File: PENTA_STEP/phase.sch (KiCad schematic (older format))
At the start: 12 parts, among them Q1 BUK9K45-100E,115, Q2 BUK9K45-100E,115

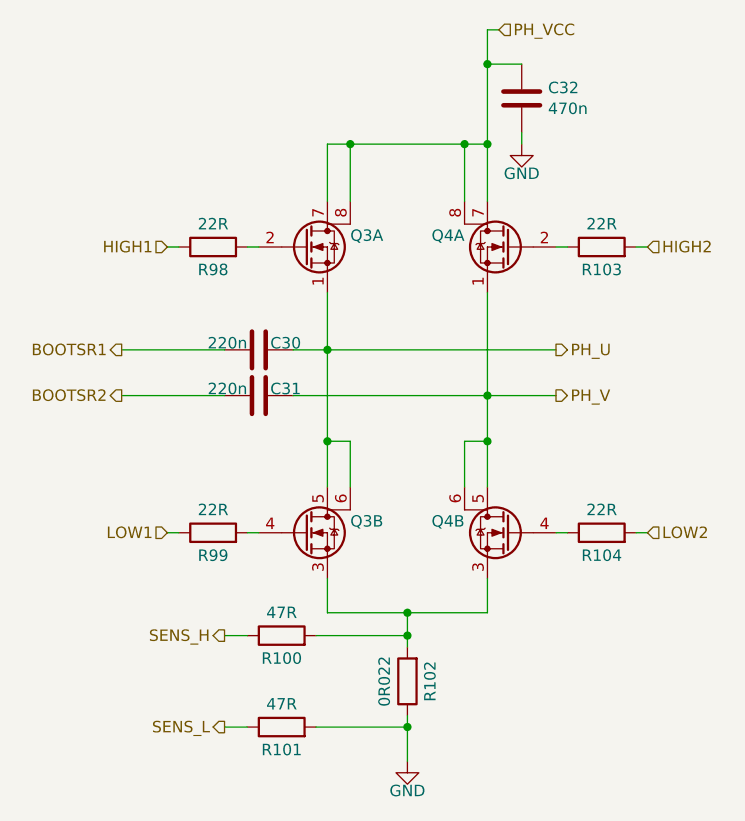
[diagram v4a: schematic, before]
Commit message: finalized BOM, found TMC5160-TA being replaced by TMC5160A-TA
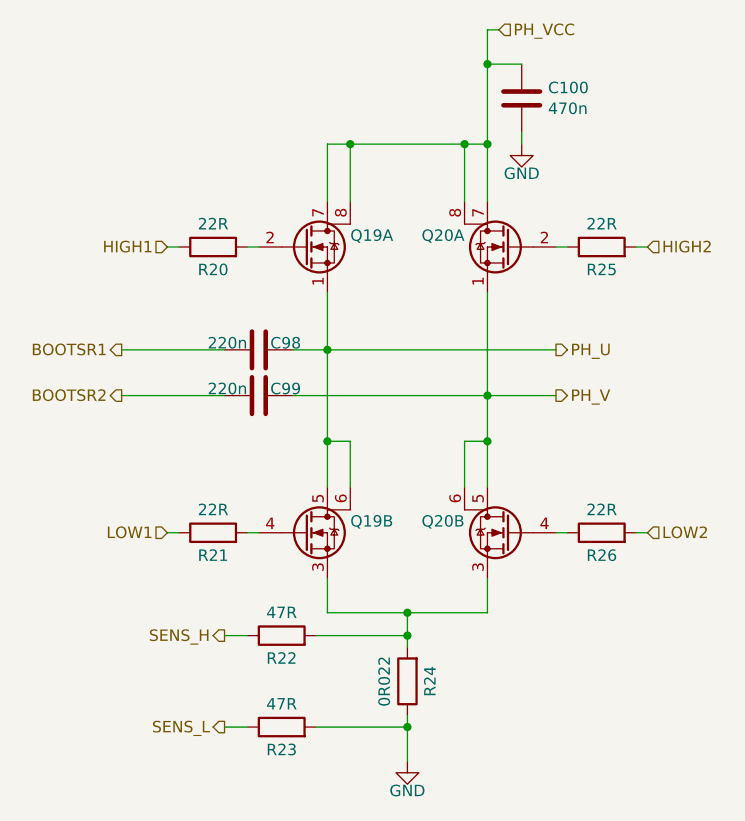
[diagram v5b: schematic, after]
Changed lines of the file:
@@
 EESchema Schematic File Version 4
-LIBS:PENTA_STEP-cache
-EELAYER 26 0
+EELAYER 30 0
 EELAYER END
 $Descr A4 11693 8268
 encoding utf-8
-Sheet 15 16
+Sheet 13 16
 Title ""
 Date ""
@@
 AR Path="/5F24B60D/5E4B900F/5E30367B" Ref="Q17"  Part="1"
 AR Path="/5F24B60D/5E4B9032/5E30367B" Ref="Q19"  Part="1"
-F 0 "Q3" H 5400 3000 50  0000 L CNN
+F 0 "Q19" H 5400 3000 50  0000 L CNN
 F 1 "BUK9K45-100E,115" H 5487 2905 50  0001 L CNN
 F 2 "CUSTOM_FP:TRANS_BUK7K12-60EX" H 5400 2875 50  0001 L CIN
@@
 AR Path="/5F24B60D/5E4B900F/5E303682" Ref="Q18"  Part="1"
 AR Path="/5F24B60D/5E4B9032/5E303682" Ref="Q20"  Part="1"
-F 0 "Q4" H 6300 3000 50  0000 L CNN
+F 0 "Q20" H 6300 3000 50  0000 L CNN
 F 1 "BUK9K45-100E,115" H 6388 2905 50  0001 L CNN
 F 2 "CUSTOM_FP:TRANS_BUK7K12-60EX" H 6300 2875 50  0001 L CIN
@@
 AR Path="/5F24B60D/5E4B900F/5E303689" Ref="Q17"  Part="2"
 AR Path="/5F24B60D/5E4B9032/5E303689" Ref="Q19"  Part="2"
-F 0 "Q3" H 5400 4250 50  0000 L CNN
+F 0 "Q19" H 5400 4250 50  0000 L CNN
 F 1 "BUK9K45-100E,115" H 5487 4155 50  0001 L CNN
 F 2 "CUSTOM_FP:TRANS_BUK7K12-60EX" H 5400 4125 50  0001 L CIN
@@
 AR Path="/5F24B60D/5E4B900F/5E303690" Ref="Q18"  Part="2"
 AR Path="/5F24B60D/5E4B9032/5E303690" Ref="Q20"  Part="2"
-F 0 "Q4" H 6300 4250 50  0000 L CNN
+F 0 "Q20" H 6300 4250 50  0000 L CNN
 F 1 "BUK9K45-100E,115" H 6388 4155 50  0001 L CNN
 F 2 "CUSTOM:TRANS_BUK7K12-60EX" H 6300 4125 50  0001 L CIN
@@
 AR Path="/5F24B60D/5E4B900F/5E303697" Ref="#PWR0109"  Part="1"
 AR Path="/5F24B60D/5E4B9032/5E303697" Ref="#PWR0111"  Part="1"
-F 0 "#PWR045" H 5650 4950 50  0001 C CNN
+F 0 "#PWR0111" H 5650 4950 50  0001 C CNN
 F 1 "GND" H 5650 5100 50  0000 C TNN
 F 2 "" H 5650 5200 50  0001 C CNN
@@
 AR Path="/5F24B60D/5E4B900F/5E30369F" Ref="R17"  Part="1"
 AR Path="/5F24B60D/5E4B9032/5E30369F" Ref="R24"  Part="1"
-F 0 "R102" V 5550 4850 50  0000 C CNN
+F 0 "R24" V 5550 4850 50  0000 C CNN
 F 1 "0R022" V 5750 4850 50  0000 C CNN
 F 2 "CUSTOM_FP:WSH2818R0500FEA" V 5580 4850 50  0001 C CNN
@@
 AR Path="/5F24B60D/5E4B900F/5E3036A9" Ref="R14"  Part="1"
 AR Path="/5F24B60D/5E4B9032/5E3036A9" Ref="R21"  Part="1"
-F 0 "R99" V 4700 4200 50  0000 C CNN
+F 0 "R21" V 4700 4200 50  0000 C CNN
 F 1 "22R" V 4900 4200 50  0000 C CNN
 F 2 "Resistor_SMD:R_0603_1608Metric_Pad1.05x0.95mm_HandSolder" V 4730 4200 50  0001 C CNN
@@
 AR Path="/5F24B60D/5E4B900F/5E3036B3" Ref="R19"  Part="1"
 AR Path="/5F24B60D/5E4B9032/5E3036B3" Ref="R26"  Part="1"
-F 0 "R104" V 6400 4200 50  0000 C CNN
+F 0 "R26" V 6400 4200 50  0000 C CNN
 F 1 "22R" V 6600 4200 50  0000 C CNN
 F 2 "Resistor_SMD:R_0603_1608Metric_Pad1.05x0.95mm_HandSolder" V 6430 4200 50  0001 C CNN
@@
 AR Path="/5F24B60D/5E4B900F/5E3036BD" Ref="R18"  Part="1"
 AR Path="/5F24B60D/5E4B9032/5E3036BD" Ref="R25"  Part="1"
-F 0 "R103" V 6400 2950 50  0000 C CNN
+F 0 "R25" V 6400 2950 50  0000 C CNN
 F 1 "22R" V 6600 2950 50  0000 C CNN
 F 2 "Resistor_SMD:R_0603_1608Metric_Pad1.05x0.95mm_HandSolder" V 6430 2950 50  0001 C CNN
@@
 AR Path="/5F24B60D/5E4B900F/5E3036C7" Ref="R13"  Part="1"
 AR Path="/5F24B60D/5E4B9032/5E3036C7" Ref="R20"  Part="1"
-F 0 "R98" V 4700 2950 50  0000 C CNN
+F 0 "R20" V 4700 2950 50  0000 C CNN
 F 1 "22R" V 4900 2950 50  0000 C CNN
 F 2 "Resistor_SMD:R_0603_1608Metric_Pad1.05x0.95mm_HandSolder" V 4730 2950 50  0001 C CNN
@@
 AR Path="/5F24B60D/5E4B900F/5E3036D1" Ref="R15"  Part="1"
 AR Path="/5F24B60D/5E4B9032/5E3036D1" Ref="R22"  Part="1"
-F 0 "R100" V 5000 4650 50  0000 C CNN
+F 0 "R22" V 5000 4650 50  0000 C CNN
 F 1 "47R" V 5200 4650 50  0000 C CNN
 F 2 "Resistor_SMD:R_0603_1608Metric_Pad1.05x0.95mm_HandSolder" V 5030 4650 50  0001 C CNN
@@
 AR Path="/5F24B60D/5E4B900F/5E3036DB" Ref="R16"  Part="1"
 AR Path="/5F24B60D/5E4B9032/5E3036DB" Ref="R23"  Part="1"
-F 0 "R101" V 5000 5050 50  0000 C CNN
+F 0 "R23" V 5000 5050 50  0000 C CNN
 F 1 "47R" V 5200 5050 50  0000 C CNN
 F 2 "Resistor_SMD:R_0603_1608Metric_Pad1.05x0.95mm_HandSolder" V 5030 5050 50  0001 C CNN
@@
 AR Path="/5F24B60D/5E4B900F/5E3036E5" Ref="C97"  Part="1"
 AR Path="/5F24B60D/5E4B9032/5E3036E5" Ref="C100"  Part="1"
-F 0 "C32" H 6265 2346 50  0000 L CNN
+F 0 "C100" H 6265 2346 50  0000 L CNN
 F 1 "470n" H 6265 2255 50  0000 L CNN
 F 2 "Capacitor_SMD:C_0603_1608Metric_Pad1.05x0.95mm_HandSolder" H 6188 2150 50  0001 C CNN
@@
 AR Path="/5F24B60D/5E4B900F/5E3036EF" Ref="C95"  Part="1"
 AR Path="/5F24B60D/5E4B9032/5E3036EF" Ref="C98"  Part="1"
-F 0 "C30" V 5000 3450 50  0000 L BNN
+F 0 "C98" V 5000 3450 50  0000 L BNN
 F 1 "220n" V 5000 3350 50  0000 R BNN
 F 2 "Capacitor_SMD:C_0603_1608Metric_Pad1.05x0.95mm_HandSolder" H 5038 3250 50  0001 C CNN
@@
 AR Path="/5F24B60D/5E4B900F/5E303702" Ref="C96"  Part="1"
 AR Path="/5F24B60D/5E4B9032/5E303702" Ref="C99"  Part="1"
-F 0 "C31" V 5000 3650 50  0000 L BNN
+F 0 "C99" V 5000 3650 50  0000 L BNN
 F 1 "220n" V 5000 3550 50  0000 R BNN
 F 2 "Capacitor_SMD:C_0603_1608Metric_Pad1.05x0.95mm_HandSolder" H 5038 3450 50  0001 C CNN
@@
 AR Path="/5F24B60D/5E4B900F/5E303736" Ref="#PWR0110"  Part="1"
 AR Path="/5F24B60D/5E4B9032/5E303736" Ref="#PWR0112"  Part="1"
-F 0 "#PWR046" H 6150 2250 50  0001 C CNN
+F 0 "#PWR0112" H 6150 2250 50  0001 C CNN
 F 1 "GND" H 6150 2400 50  0000 C TNN
 F 2 "" H 6150 2500 50  0001 C CNN
